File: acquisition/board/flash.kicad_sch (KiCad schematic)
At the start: 5 parts

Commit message: Continued initial design
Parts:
- gave numbers to parts that had none: 5
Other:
- company: (none) -> A. Zonenberg
- title: (none) -> Digitizer board
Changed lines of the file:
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@@
 (kicad_sch (version 20211123) (generator eeschema)
   (paper "A4")
+  (title_block
+    (title "Digitizer board")
+    (date "2022-06-22")
+    (rev "0.1")
+    (company "A. Zonenberg")
+  )
   (wire (pts (xy 114.3 54.61) (xy 121.92 54.61))
     (stroke (width 0) (type default) (color 0 0 0 0))
@@
   (symbol (lib_id "device:R") (at 110.49 57.15 90) (unit 1)
     (in_bom yes) (on_board yes)
-    (property "Reference" "R?" (id 0) (at 116.84 55.88 90))
+    (property "Reference" "R7" (id 0) (at 116.84 55.88 90))
     (property "Value" "33" (id 1) (at 110.49 57.15 90))
     (property "Footprint" "" (id 2) (at 110.49 58.928 90)
@@
   (symbol (lib_id "device:R") (at 110.49 54.61 90) (unit 1)
     (in_bom yes) (on_board yes)
-    (property "Reference" "R?" (id 0) (at 116.84 53.34 90))
+    (property "Reference" "R6" (id 0) (at 116.84 53.34 90))
     (property "Value" "33" (id 1) (at 110.49 54.61 90))
     (property "Footprint" "" (id 2) (at 110.49 56.388 90)
@@
   (symbol (lib_id "device:R") (at 110.49 52.07 90) (unit 1)
     (in_bom yes) (on_board yes)
-    (property "Reference" "R?" (id 0) (at 116.84 50.8 90))
+    (property "Reference" "R5" (id 0) (at 116.84 50.8 90))
     (property "Value" "33" (id 1) (at 110.49 52.07 90))
     (property "Footprint" "" (id 2) (at 110.49 53.848 90)
@@
   (symbol (lib_id "memory-azonenberg:S25FLxxxS_BGA24_5x5_VIO") (at 74.93 63.5 0) (unit 1)
     (in_bom yes) (on_board yes) (fields_autoplaced)
-    (property "Reference" "U?" (id 0) (at 88.265 38.7761 0)
+    (property "Reference" "U9" (id 0) (at 88.265 38.7761 0)
       (effects (font (size 1.524 1.524)))
     )
@@
   (symbol (lib_id "device:R") (at 110.49 49.53 90) (unit 1)
     (in_bom yes) (on_board yes)
-    (property "Reference" "R?" (id 0) (at 116.84 48.26 90))
+    (property "Reference" "R4" (id 0) (at 116.84 48.26 90))
     (property "Value" "33" (id 1) (at 110.49 49.53 90))
     (property "Footprint" "" (id 2) (at 110.49 51.308 90)

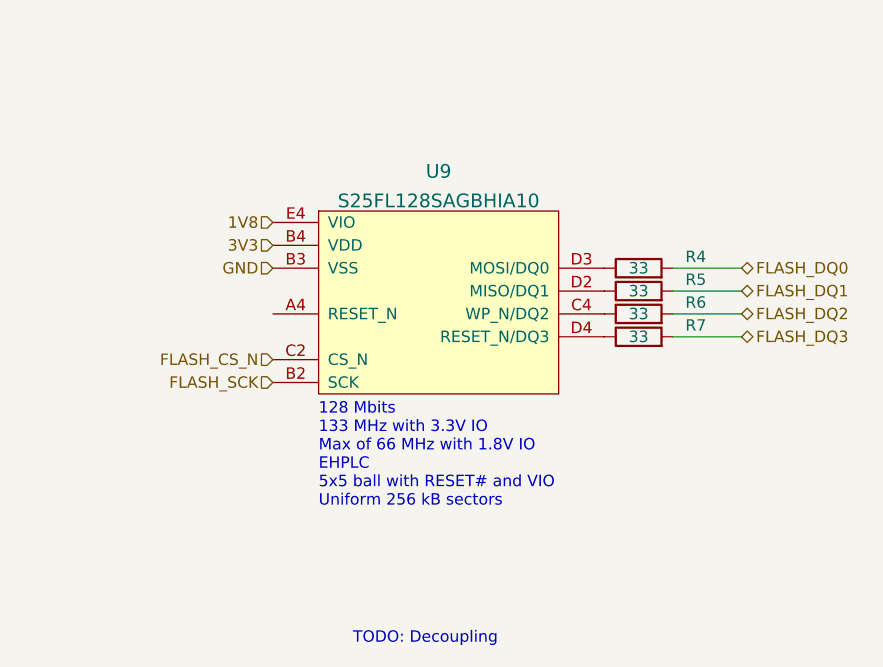
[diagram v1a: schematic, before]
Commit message: Updated schematic with a lot of level shifting and support stuff, power decoupling, etc. Almost done except power supply and protection diodes
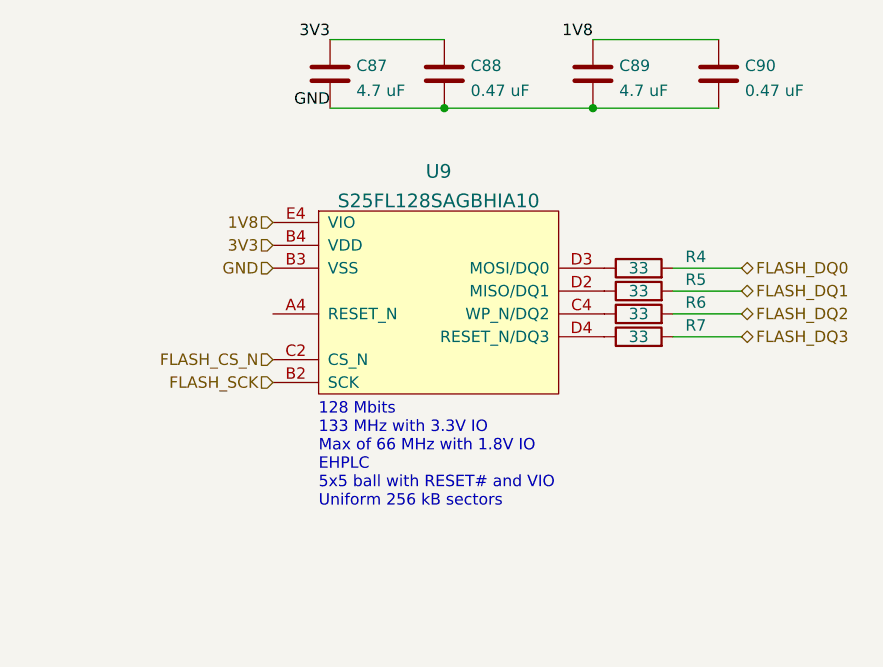
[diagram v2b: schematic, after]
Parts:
- added C87, C89: 4.7 uF, symbol device:C
- added C88, C90: 0.47 uF, symbol device:C
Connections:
- net 1V8: now also C89.1, C90.1
- net 3V3: now also C87.1, C88.1
- net GND: now also C87.2, C88.2, C89.2, C90.2
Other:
- note removed: "TODO: Decoupling"
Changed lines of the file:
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@@
   (title_block
     (title "Digitizer board")
-    (date "2022-06-22")
+    (date "2022-07-04")
     (rev "0.1")
     (company "A. Zonenberg")
   )
+  (junction (at 88.9 31.75) (diameter 0) (color 0 0 0 0)
+  )
+  (junction (at 105.41 31.75) (diameter 0) (color 0 0 0 0)
+  )
   (wire (pts (xy 114.3 54.61) (xy 121.92 54.61))
     (stroke (width 0) (type default) (color 0 0 0 0))
   )
+  (wire (pts (xy 105.41 24.13) (xy 119.38 24.13))
+    (stroke (width 0) (type default) (color 0 0 0 0))
+  )
   (wire (pts (xy 114.3 57.15) (xy 121.92 57.15))
     (stroke (width 0) (type default) (color 0 0 0 0))
   )
+  (wire (pts (xy 105.41 31.75) (xy 119.38 31.75))
+    (stroke (width 0) (type default) (color 0 0 0 0))
+  )
+  (wire (pts (xy 76.2 24.13) (xy 88.9 24.13))
+    (stroke (width 0) (type default) (color 0 0 0 0))
+  )
+  (wire (pts (xy 88.9 31.75) (xy 105.41 31.75))
+    (stroke (width 0) (type default) (color 0 0 0 0))
+  )
+  (wire (pts (xy 76.2 31.75) (xy 88.9 31.75))
+    (stroke (width 0) (type default) (color 0 0 0 0))
+  )
   (wire (pts (xy 114.3 49.53) (xy 121.92 49.53))
     (stroke (width 0) (type default) (color 0 0 0 0))
@@
   (wire (pts (xy 114.3 52.07) (xy 121.92 52.07))
     (stroke (width 0) (type default) (color 0 0 0 0))
-  )
-  (text "TODO: Decoupling" (at 78.74 91.44 0)
-    (effects (font (size 1.27 1.27)) (justify left bottom))
   )
   (text "128 Mbits\n133 MHz with 3.3V IO\nMax of 66 MHz with 1.8V IO\nEHPLC\n5x5 ball with RESET# and VIO\nUniform 256 kB sectors"
@@
     (effects (font (size 1.27 1.27)) (justify left bottom))
   )
+  (label "1V8" (at 105.41 24.13 180)
+    (effects (font (size 1.27 1.27)) (justify right bottom))
+  )
+  (label "GND" (at 76.2 31.75 180)
+    (effects (font (size 1.27 1.27)) (justify right bottom))
+  )
+  (label "3V3" (at 76.2 24.13 180)
+    (effects (font (size 1.27 1.27)) (justify right bottom))
+  )
   (hierarchical_label "FLASH_DQ1" (shape bidirectional) (at 121.92 52.07 0)
     (effects (font (size 1.27 1.27)) (justify left))
@@
   (hierarchical_label "3V3" (shape input) (at 69.85 46.99 180)
     (effects (font (size 1.27 1.27)) (justify right))
+  )
+  (symbol (lib_id "device:C") (at 119.38 27.94 0) (unit 1)
+    (in_bom yes) (on_board yes) (fields_autoplaced)
+    (property "Reference" "C90" (id 0) (at 122.301 27.0315 0)
+      (effects (font (size 1.27 1.27)) (justify left))
+    )
+    (property "Value" "0.47 uF" (id 1) (at 122.301 29.8066 0)
+      (effects (font (size 1.27 1.27)) (justify left))
+    )
+    (property "Footprint" "" (id 2) (at 120.3452 31.75 0)
+      (effects (font (size 1.27 1.27)) hide)
+    )
+    (property "Datasheet" "" (id 3) (at 119.38 27.94 0)
+      (effects (font (size 1.27 1.27)) hide)
+    )
+    (pin "1")
+    (pin "2")
   )
   (symbol (lib_id "device:R") (at 110.49 57.15 90) (unit 1)
@@
     )
     (property "Datasheet" "" (id 3) (at 110.49 57.15 0)
+      (effects (font (size 1.27 1.27)) hide)
+    )
+    (pin "1")
+    (pin "2")
+  )
+  (symbol (lib_id "device:C") (at 88.9 27.94 0) (unit 1)
+    (in_bom yes) (on_board yes) (fields_autoplaced)
+    (property "Reference" "C88" (id 0) (at 91.821 27.0315 0)
+      (effects (font (size 1.27 1.27)) (justify left))
+    )
+    (property "Value" "0.47 uF" (id 1) (at 91.821 29.8066 0)
+      (effects (font (size 1.27 1.27)) (justify left))
+    )
+    (property "Footprint" "" (id 2) (at 89.8652 31.75 0)
+      (effects (font (size 1.27 1.27)) hide)
+    )
+    (property "Datasheet" "" (id 3) (at 88.9 27.94 0)
+      (effects (font (size 1.27 1.27)) hide)
+    )
+    (pin "1")
+    (pin "2")
+  )
+  (symbol (lib_id "device:C") (at 105.41 27.94 0) (unit 1)
+    (in_bom yes) (on_board yes) (fields_autoplaced)
+    (property "Reference" "C89" (id 0) (at 108.331 27.0315 0)
+      (effects (font (size 1.27 1.27)) (justify left))
+    )
+    (property "Value" "4.7 uF" (id 1) (at 108.331 29.8066 0)
+      (effects (font (size 1.27 1.27)) (justify left))
+    )
+    (property "Footprint" "" (id 2) (at 106.3752 31.75 0)
+      (effects (font (size 1.27 1.27)) hide)
+    )
+    (property "Datasheet" "" (id 3) (at 105.41 27.94 0)
       (effects (font (size 1.27 1.27)) hide)
     )
@@
       (effects (font (size 1.27 1.27)) hide)
     )
+    (pin "1")
+    (pin "2")
+  )
+  (symbol (lib_id "device:C") (at 76.2 27.94 0) (unit 1)
+    (in_bom yes) (on_board yes) (fields_autoplaced)
+    (property "Reference" "C87" (id 0) (at 79.121 27.0315 0)
+      (effects (font (size 1.27 1.27)) (justify left))
+    )
+    (property "Value" "4.7 uF" (id 1) (at 79.121 29.8066 0)
+      (effects (font (size 1.27 1.27)) (justify left))
+    )
+    (property "Footprint" "" (id 2) (at 77.1652 31.75 0)
+      (effects (font (size 1.27 1.27)) hide)
+    )
+    (property "Datasheet" "" (id 3) (at 76.2 27.94 0)
+      (effects (font (size 1.27 1.27)) hide)
+    )

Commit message: More power supply work, added PLL loop filter, soft start, began assigning footprints
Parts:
- added R80: 10K, symbol device:R
- C87, C89: footprint (none) -> azonenberg_pcb:EIA_0603_CAP_NOSILK
- C88, C90: footprint (none) -> azonenberg_pcb:EIA_0402_CAP_NOSILK
- R4, R5, R6, R7: footprint (none) -> azonenberg_pcb:EIA_0402_RES_NOSILK
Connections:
- net 1V8: now also R80.1
- net at U9.A4 (RESET_N): now also R80.2
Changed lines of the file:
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@@
   (title_block
     (title "Digitizer board")
-    (date "2022-07-05")
+    (date "2022-07-08")
     (rev "0.1")
     (company "A. Zonenberg")
@@
   )
   (wire (pts (xy 114.3 52.07) (xy 121.92 52.07))
+    (stroke (width 0) (type default) (color 0 0 0 0))
+  )
+  (wire (pts (xy 62.23 54.61) (xy 69.85 54.61))
     (stroke (width 0) (type default) (color 0 0 0 0))
   )
@@
     (effects (font (size 1.27 1.27)) (justify left bottom))
   )
+  (label "1V8" (at 54.61 54.61 180)
+    (effects (font (size 1.27 1.27)) (justify right bottom))
+  )
   (label "1V8" (at 105.41 24.13 180)
     (effects (font (size 1.27 1.27)) (justify right bottom))
@@
       (effects (font (size 1.27 1.27)) (justify left))
     )
-    (property "Footprint" "" (id 2) (at 120.3452 31.75 0)
+    (property "Footprint" "azonenberg_pcb:EIA_0402_CAP_NOSILK" (id 2) (at 120.3452 31.75 0)
       (effects (font (size 1.27 1.27)) hide)
     )
@@
     (property "Reference" "R7" (id 0) (at 116.84 55.88 90))
     (property "Value" "33" (id 1) (at 110.49 57.15 90))
-    (property "Footprint" "" (id 2) (at 110.49 58.928 90)
+    (property "Footprint" "azonenberg_pcb:EIA_0402_RES_NOSILK" (id 2) (at 110.49 58.928 90)
       (effects (font (size 1.27 1.27)) hide)
     )
@@
     (pin "2")
   )
+  (symbol (lib_id "device:R") (at 58.42 54.61 90) (unit 1)
+    (in_bom yes) (on_board yes)
+    (property "Reference" "R80" (id 0) (at 58.42 52.07 90))
+    (property "Value" "10K" (id 1) (at 58.42 54.61 90))
+    (property "Footprint" "" (id 2) (at 58.42 56.388 90)
+      (effects (font (size 1.27 1.27)) hide)
+    )
+    (property "Datasheet" "" (id 3) (at 58.42 54.61 0)
+      (effects (font (size 1.27 1.27)) hide)
+    )
+    (pin "1")
+    (pin "2")
+  )
   (symbol (lib_id "device:C") (at 88.9 27.94 0) (unit 1)
     (in_bom yes) (on_board yes) (fields_autoplaced)
@@
       (effects (font (size 1.27 1.27)) (justify left))
     )
-    (property "Footprint" "" (id 2) (at 89.8652 31.75 0)
+    (property "Footprint" "azonenberg_pcb:EIA_0402_CAP_NOSILK" (id 2) (at 89.8652 31.75 0)
       (effects (font (size 1.27 1.27)) hide)
     )
@@
       (effects (font (size 1.27 1.27)) (justify left))
     )
-    (property "Footprint" "" (id 2) (at 106.3752 31.75 0)
+    (property "Footprint" "azonenberg_pcb:EIA_0603_CAP_NOSILK" (id 2) (at 106.3752 31.75 0)
       (effects (font (size 1.27 1.27)) hide)
     )
@@
     (property "Reference" "R6" (id 0) (at 116.84 53.34 90))
     (property "Value" "33" (id 1) (at 110.49 54.61 90))
-    (property "Footprint" "" (id 2) (at 110.49 56.388 90)
+    (property "Footprint" "azonenberg_pcb:EIA_0402_RES_NOSILK" (id 2) (at 110.49 56.388 90)
       (effects (font (size 1.27 1.27)) hide)
     )
@@
     (property "Reference" "R5" (id 0) (at 116.84 50.8 90))
     (property "Value" "33" (id 1) (at 110.49 52.07 90))
-    (property "Footprint" "" (id 2) (at 110.49 53.848 90)
+    (property "Footprint" "azonenberg_pcb:EIA_0402_RES_NOSILK" (id 2) (at 110.49 53.848 90)
       (effects (font (size 1.27 1.27)) hide)
     )
@@
     (property "Reference" "R4" (id 0) (at 116.84 48.26 90))
     (property "Value" "33" (id 1) (at 110.49 49.53 90))
-    (property "Footprint" "" (id 2) (at 110.49 51.308 90)
+    (property "Footprint" "azonenberg_pcb:EIA_0402_RES_NOSILK" (id 2) (at 110.49 51.308 90)
       (effects (font (size 1.27 1.27)) hide)
     )
@@
       (effects (font (size 1.27 1.27)) (justify left))
     )
-    (property "Footprint" "" (id 2) (at 77.1652 31.75 0)
-      (effects (font (size 1.27 1.27)) hide)
-    )
+    (property "Footprint" "azonenberg_pcb:EIA_0603_CAP_NOSILK" (id 2) (at 77.1652 31.75 0)
+      (effects (font (size 1.27 1.27)) hide)
+    )

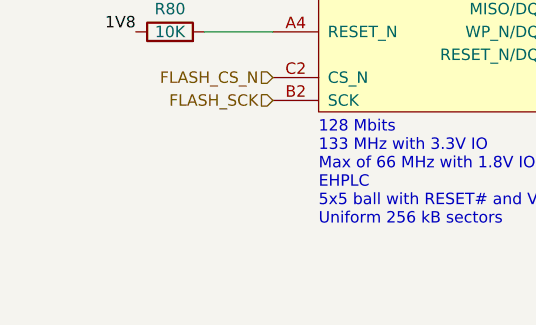
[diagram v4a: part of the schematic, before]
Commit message: Completed schematic after design review, ready for layout
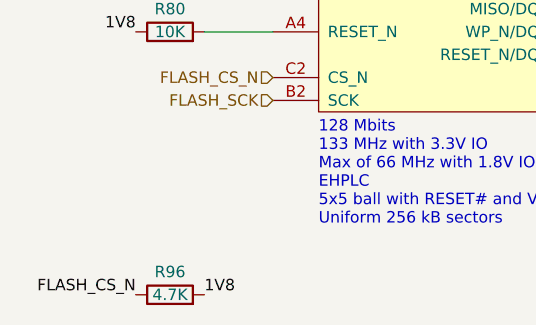
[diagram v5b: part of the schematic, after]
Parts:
- added R96: 4.7K, azonenberg_pcb:EIA_0402_RES_NOSILK, symbol device:R
- R80: footprint (none) -> azonenberg_pcb:EIA_0402_RES_NOSILK
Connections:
- net 1V8: now also R96.2
- net FLASH_CS_N: now also R96.1
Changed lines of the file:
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@@
   (title_block
     (title "Digitizer board")
-    (date "2022-07-08")
+    (date "2022-07-17")
     (rev "0.1")
     (company "A. Zonenberg")
@@
   (label "GND" (at 76.2 31.75 180)
     (effects (font (size 1.27 1.27)) (justify right bottom))
+  )
+  (label "FLASH_CS_N" (at 54.61 83.82 180)
+    (effects (font (size 1.27 1.27)) (justify right bottom))
+  )
+  (label "1V8" (at 62.23 83.82 0)
+    (effects (font (size 1.27 1.27)) (justify left bottom))
   )
   (label "3V3" (at 76.2 24.13 180)
@@
     (pin "2")
   )
+  (symbol (lib_id "device:R") (at 58.42 83.82 90) (unit 1)
+    (in_bom yes) (on_board yes)
+    (property "Reference" "R96" (id 0) (at 58.42 81.28 90))
+    (property "Value" "4.7K" (id 1) (at 58.42 83.82 90))
+    (property "Footprint" "azonenberg_pcb:EIA_0402_RES_NOSILK" (id 2) (at 58.42 85.598 90)
+      (effects (font (size 1.27 1.27)) hide)
+    )
+    (property "Datasheet" "" (id 3) (at 58.42 83.82 0)
+      (effects (font (size 1.27 1.27)) hide)
+    )
+    (pin "1")
+    (pin "2")
+  )
   (symbol (lib_id "device:R") (at 58.42 54.61 90) (unit 1)
     (in_bom yes) (on_board yes)
     (property "Reference" "R80" (id 0) (at 58.42 52.07 90))
     (property "Value" "10K" (id 1) (at 58.42 54.61 90))
-    (property "Footprint" "" (id 2) (at 58.42 56.388 90)
+    (property "Footprint" "azonenberg_pcb:EIA_0402_RES_NOSILK" (id 2) (at 58.42 56.388 90)
       (effects (font (size 1.27 1.27)) hide)
     )

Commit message: Finished footprint assignment
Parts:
- U9: footprint (none) -> azonenberg_pcb:BGA_24_6x8_DEPOP1_1MM
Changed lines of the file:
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@@
   (title_block
     (title "Digitizer board")
-    (date "2022-07-17")
+    (date "2023-01-29")
     (rev "0.1")
     (company "A. Zonenberg")
@@
       (effects (font (size 1.524 1.524)))
     )
-    (property "Footprint" "" (id 2) (at 74.93 63.5 0)
+    (property "Footprint" "azonenberg_pcb:BGA_24_6x8_DEPOP1_1MM" (id 2) (at 74.93 63.5 0)
       (effects (font (size 1.524 1.524)) hide)
     )
